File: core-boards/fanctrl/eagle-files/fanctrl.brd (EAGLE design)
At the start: 50.8 x 50.8 mm, 31 parts, among them J1 3-PIN_2MM-H, U1 MCP9701T-E/TT

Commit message: Fix typo: ISCP --> ICSP.
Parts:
- JP1: value ISCP -> ICSP
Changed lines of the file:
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@@
 <attribute name="SPICEPREFIX" value="R" x="16.875" y="42.75" size="1.778" layer="27" rot="R270" display="off"/>
 </element>
-<element name="JP1" library="pinhead" library_urn="urn:adsk.eagle:library:325" package="2X03" package3d_urn="urn:adsk.eagle:package:22462/2" value="ISCP" x="47" y="21.6" smashed="yes" rot="R90">
+<element name="JP1" library="pinhead" library_urn="urn:adsk.eagle:library:325" package="2X03" package3d_urn="urn:adsk.eagle:package:22462/2" value="ICSP" x="47" y="21.6" smashed="yes" rot="R90">
 <attribute name="NAME" x="44.32" y="25.905" size="0.6096" layer="25" ratio="10"/>
 <attribute name="POPULARITY" value="62" x="47" y="21.6" size="1.778" layer="27" rot="R90" display="off"/>

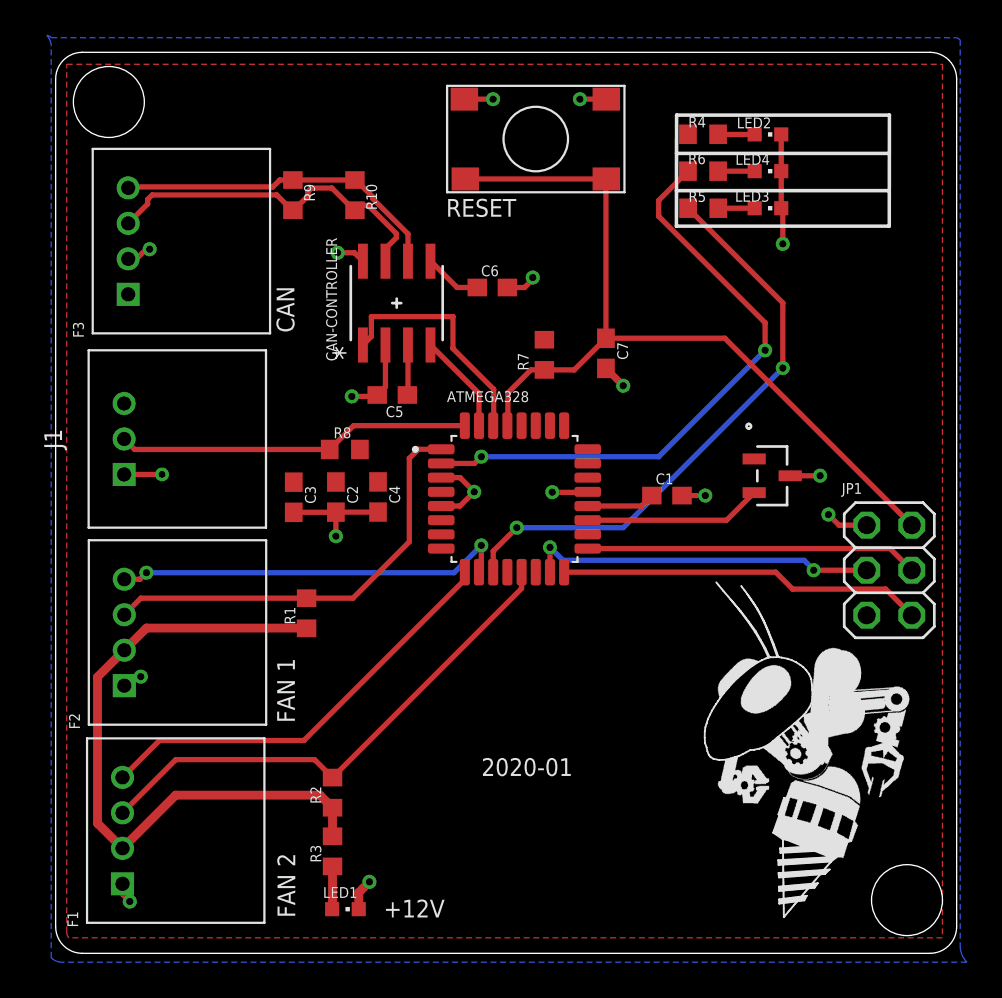
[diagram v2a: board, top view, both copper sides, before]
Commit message: Jank jumper for CAN resistor added.
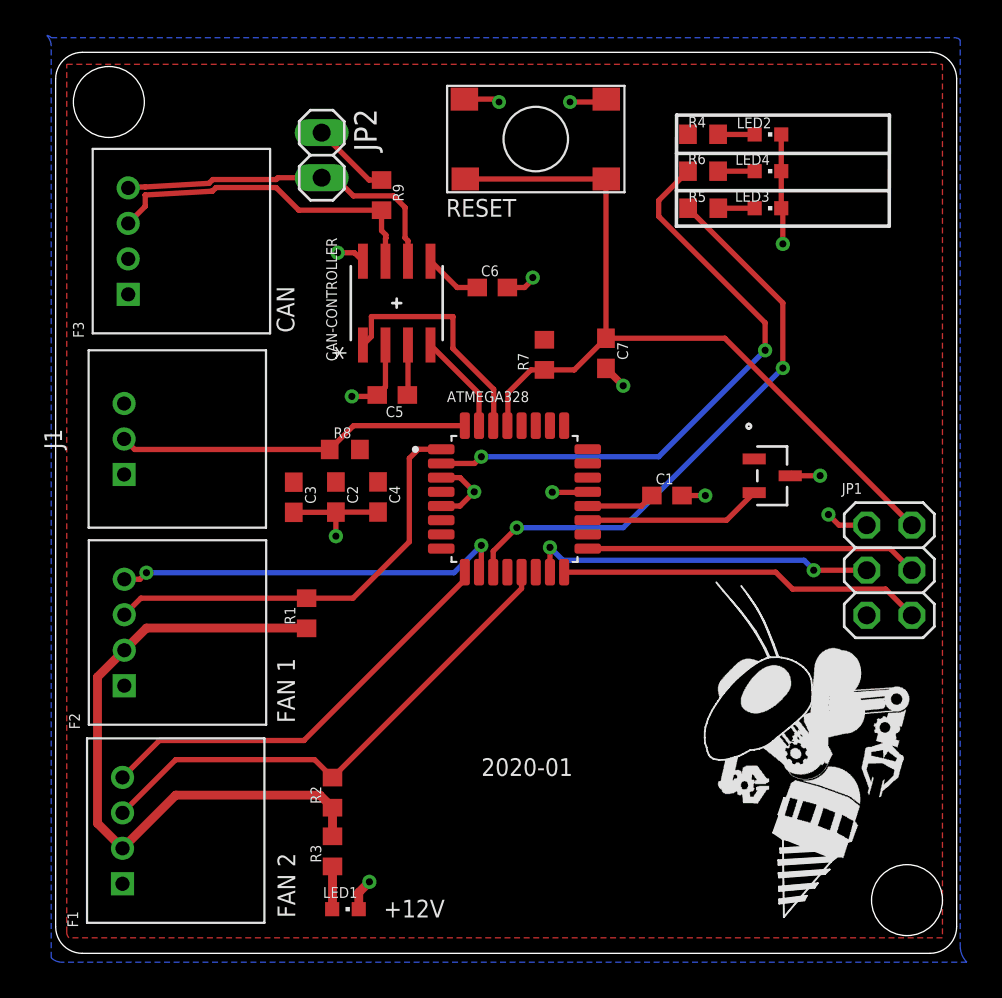
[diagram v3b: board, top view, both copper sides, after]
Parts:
- removed R10: 120Ω, rcl:R0603
- added JP2: (no value), pinhead:1X02
- moved R9 5.00 mm to (18.4, 42.8)
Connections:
- new net N$1: JP2.1, R9.1
- net CAN_N: now also JP2.2; no longer R10.1, R9.1
- net CAN_P: no longer R10.2
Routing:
- net GND: track 44.6 -> 39.7 mm, vias 18 -> 14
- net N$1: track 0.00 -> 4.48 mm
- net CAN_P: track 20.1 -> 18.9 mm
- net CAN_N: track 18.8 -> 18.0 mm

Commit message: Fix LED Resist. values --> 470ohm
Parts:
- R3: value 2.2K -> 470Ω
- R4, R5, R6: value 1K -> 470Ω
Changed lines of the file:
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@@
 <attribute name="SPICEPREFIX" value="C" x="18.175" y="25.73" size="1.778" layer="27" rot="R270" display="off"/>
 </element>
-<element name="R3" library="rcl" library_urn="urn:adsk.eagle:library:334" package="R0603" package3d_urn="urn:adsk.eagle:package:23555/3" value="2.2K" x="15.61" y="5.75" smashed="yes" rot="R90">
+<element name="R3" library="rcl" library_urn="urn:adsk.eagle:library:334" package="R0603" package3d_urn="urn:adsk.eagle:package:23555/3" value="470Ω" x="15.61" y="5.75" smashed="yes" rot="R90">
 <attribute name="NAME" x="14.975" y="5.115" size="0.6096" layer="25" rot="R90"/>
 <attribute name="POPULARITY" value="77" x="15.61" y="5.75" size="1.778" layer="27" rot="R90" display="off"/>
 <attribute name="SPICEPREFIX" value="R" x="15.61" y="5.75" size="1.778" layer="27" rot="R90" display="off"/>
 </element>
-<element name="R4" library="rcl" library_urn="urn:adsk.eagle:library:334" package="R0603" package3d_urn="urn:adsk.eagle:package:23555/3" value="1K" x="36.5" y="46.18" smashed="yes" rot="R180">
+<element name="R4" library="rcl" library_urn="urn:adsk.eagle:library:334" package="R0603" package3d_urn="urn:adsk.eagle:package:23555/3" value="470Ω" x="36.5" y="46.18" smashed="yes" rot="R180">
 <attribute name="NAME" x="35.665" y="46.565" size="0.6096" layer="25"/>
 <attribute name="POPULARITY" value="77" x="36.5" y="46.18" size="1.778" layer="27" rot="R180" display="off"/>
@@
 <attribute name="POPULARITY" value="28" x="40.16" y="46.17" size="1.778" layer="27" rot="R270" display="off"/>
 </element>
-<element name="R5" library="rcl" library_urn="urn:adsk.eagle:library:334" package="R0603" package3d_urn="urn:adsk.eagle:package:23555/3" value="1K" x="36.51" y="42.01" smashed="yes" rot="R180">
+<element name="R5" library="rcl" library_urn="urn:adsk.eagle:library:334" package="R0603" package3d_urn="urn:adsk.eagle:package:23555/3" value="470Ω" x="36.51" y="42.01" smashed="yes" rot="R180">
 <attribute name="NAME" x="35.675" y="42.365" size="0.6096" layer="25"/>
 <attribute name="POPULARITY" value="77" x="36.51" y="33.12" size="1.778" layer="27" rot="R180" display="off"/>
@@
 <attribute name="POPULARITY" value="28" x="43.97" y="47.09" size="1.778" layer="27" rot="R270" display="off"/>
 </element>
-<element name="R6" library="rcl" library_urn="urn:adsk.eagle:library:334" package="R0603" package3d_urn="urn:adsk.eagle:package:23555/3" value="1K" x="36.5" y="44.1" smashed="yes" rot="R180">
+<element name="R6" library="rcl" library_urn="urn:adsk.eagle:library:334" package="R0603" package3d_urn="urn:adsk.eagle:package:23555/3" value="470Ω" x="36.5" y="44.1" smashed="yes" rot="R180">
 <attribute name="NAME" x="35.655" y="44.495" size="0.6096" layer="25"/>
 <attribute name="POPULARITY" value="77" x="36.5" y="37.75" size="1.778" layer="27" rot="R180" display="off"/>

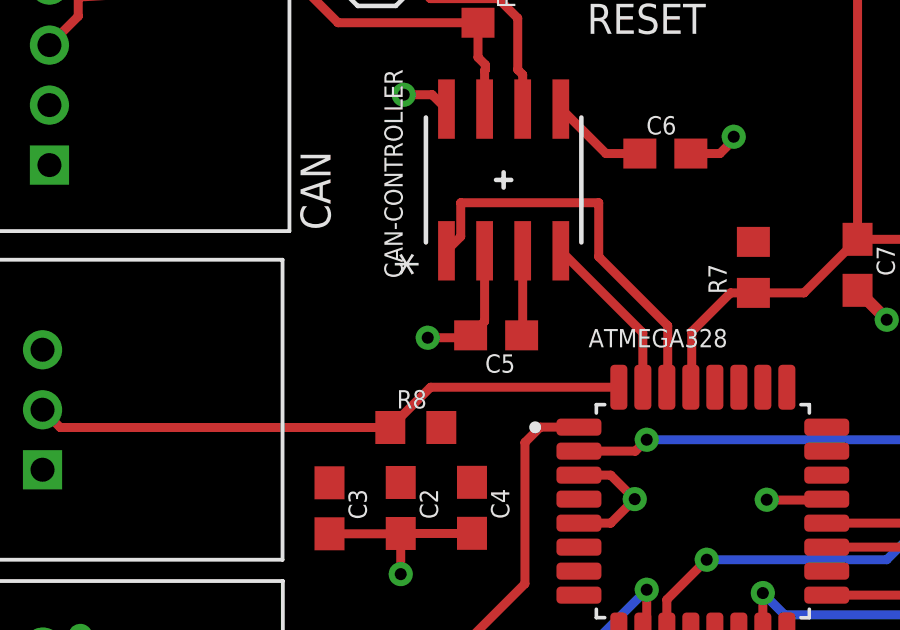
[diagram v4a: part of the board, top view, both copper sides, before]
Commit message: Add 3A fuse to +5V from CAN bus.
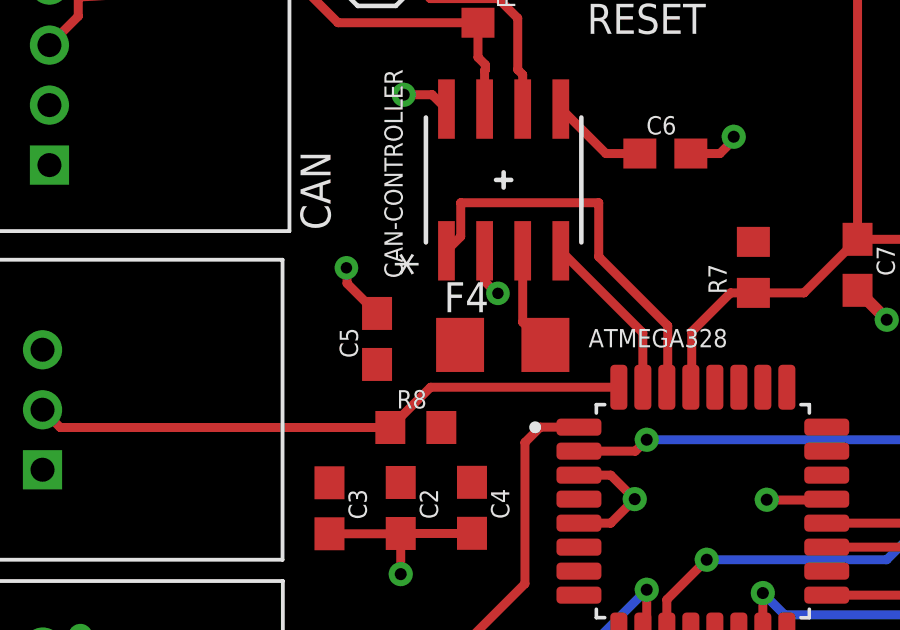
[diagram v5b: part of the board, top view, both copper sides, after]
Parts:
- added F4: 3A, RoboJackets-Fuses:F1206
- moved C5 3.97 mm to (15.0, 31.4), turned to 90 degrees
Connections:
- new net N$6: CAN-CONTROLLER.3, F4.2
- net +5V: now also F4.1; no longer CAN-CONTROLLER.3
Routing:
- net N$6: track 0.00 -> 3.45 mm
- net +5V: track 2.83 -> 0.00 mm
- net GND: track 39.7 -> 39.3 mm, vias 14 -> 15
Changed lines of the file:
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@@
 <attribute name="VENDOR" value="Microchip" x="19.23" y="36.66" size="1.778" layer="27" rot="R90" display="off"/>
 </element>
-<element name="C5" library="rcl" library_urn="urn:adsk.eagle:library:334" package="C0603" package3d_urn="urn:adsk.eagle:package:23616/2" value="0.1µF" x="18.98" y="31.48" smashed="yes" rot="R180">
-<attribute name="NAME" x="19.615" y="30.845" size="0.6096" layer="25" rot="R180"/>
-<attribute name="POPULARITY" value="37" x="18.98" y="31.48" size="1.778" layer="27" rot="R180" display="off"/>
-<attribute name="SPICEPREFIX" value="C" x="18.98" y="31.48" size="1.778" layer="27" rot="R180" display="off"/>
+<element name="C5" library="rcl" library_urn="urn:adsk.eagle:library:334" package="C0603" package3d_urn="urn:adsk.eagle:package:23616/2" value="0.1µF" x="15.01" y="31.36" smashed="yes" rot="R90">
+<attribute name="NAME" x="14.375" y="30.725" size="0.6096" layer="25" rot="R90"/>
+<attribute name="POPULARITY" value="37" x="15.01" y="31.36" size="1.778" layer="27" rot="R90" display="off"/>
+<attribute name="SPICEPREFIX" value="C" x="15.01" y="31.36" size="1.778" layer="27" rot="R90" display="off"/>
 </element>
 <element name="C6" library="rcl" library_urn="urn:adsk.eagle:library:334" package="C0603" package3d_urn="urn:adsk.eagle:package:23616/2" value="0.1µF" x="24.62" y="37.54" smashed="yes">
@@
 <attribute name="SPICEPREFIX" value="B" x="15" y="45" size="1.778" layer="27" rot="R270" display="off"/>
 <attribute name="VALUE" x="11.825" y="47.54" size="1.27" layer="27" rot="R270"/>
+</element>
+<element name="F4" library="RoboJackets-Fuses" package="F1206" value="3A" x="19.2" y="31.16" smashed="yes">
+<attribute name="NAME" x="17.24" y="32.25" size="1" layer="25"/>
 </element>
 </elements>
@@
 <wire x1="26.9" y1="38" x2="26.9" y2="38.1" width="0.3" layer="1"/>
 <via x="26.9" y="38.1" extent="1-16" drill="0.4"/>
-<wire x1="18.13" y1="31.48" x2="18.05" y2="31.4" width="0.3" layer="1"/>
-<via x="16.7" y="31.4" extent="1-16" drill="0.4"/>
-<wire x1="18.05" y1="31.4" x2="16.7" y2="31.4" width="0.3" layer="1"/>
 <wire x1="13.425" y1="24.865" x2="15.69" y2="24.865" width="0.3" layer="1"/>
 <wire x1="15.74" y1="24.815" x2="15.69" y2="24.865" width="0.3" layer="1"/>
@@
 <wire x1="35.315" y1="25.81" x2="36.63" y2="25.81" width="0.3" layer="1"/>
 <via x="36.63" y="25.81" extent="1-16" drill="0.4"/>
-<wire x1="18.595" y1="34.2978" x2="18.595" y2="31.945" width="0.3" layer="1"/>
-<wire x1="18.595" y1="31.945" x2="18.13" y2="31.48" width="0.3" layer="1"/>
+<wire x1="18.595" y1="34.2978" x2="18.725" y2="34.1678" width="0.3" layer="1"/>
+<wire x1="18.725" y1="34.1678" x2="18.725" y2="33.885" width="0.3" layer="1"/>
 <wire x1="40.91" y1="46.17" x2="40.91" y2="44.1" width="0.3" layer="1"/>
 <wire x1="40.91" y1="44.1" x2="40.91" y2="42.01" width="0.3" layer="1"/>
@@
 <wire x1="30.885" y1="48" x2="29" y2="48" width="0.3" layer="1"/>
 <via x="29" y="48" extent="1-16" drill="0.381"/>
+<wire x1="15.01" y1="32.21" x2="14.01" y2="33.21" width="0.3" layer="1"/>
+<wire x1="14.01" y1="33.21" x2="14.01" y2="33.73" width="0.3" layer="1"/>
+<wire x1="14.01" y1="33.73" x2="13.99" y2="33.73" width="0.3" layer="1"/>
+<via x="13.99" y="33.73" extent="1-16" drill="0.381"/>
+<wire x1="18.595" y1="34.2978" x2="18.595" y2="33.285" width="0.3" layer="1"/>
+<wire x1="18.595" y1="33.285" x2="19.02" y2="32.86" width="0.3" layer="1"/>
+<wire x1="19.02" y1="32.86" x2="19.04" y2="32.88" width="0.3" layer="1"/>
+<via x="19.04" y="32.88" extent="1-16" drill="0.381"/>
+<wire x1="31.045" y1="48.16" x2="40.91" y2="46.17" width="0" layer="19" extent="1-1"/>
+<wire x1="25" y1="48" x2="29" y2="48" width="0" layer="19" extent="1-1"/>
+<wire x1="26.9" y1="38.1" x2="25" y2="48" width="0" layer="19" extent="1-1"/>
+<wire x1="31.027" y1="32.98" x2="26.9" y2="38.1" width="0" layer="19" extent="1-1"/>
+<wire x1="30" y1="26.02" x2="32" y2="32" width="0" layer="19" extent="1-1"/>
+<wire x1="23.6" y1="26.02" x2="28" y2="26" width="0" layer="19" extent="1-1"/>
+<wire x1="18.245" y1="24.95" x2="21.74" y2="25.22" width="0" layer="19" extent="1-1"/>
+<wire x1="35.315" y1="25.81" x2="30" y2="26.02" width="0" layer="19" extent="1-1"/>
+<wire x1="41.4152" y1="26.925" x2="36.63" y2="25.81" width="0" layer="19" extent="1-1"/>
+<wire x1="43.57" y1="24.74" x2="43.1" y2="26.93" width="0" layer="19" extent="1-1"/>
+<wire x1="19.04" y1="32.88" x2="21.74" y2="26.82" width="0" layer="19" extent="1-1"/>
+<wire x1="15.01" y1="32.21" x2="18.725" y2="33.885" width="0" layer="19" extent="1-1"/>
+<wire x1="17.325" y1="39.0222" x2="18.595" y2="34.2978" width="0" layer="19" extent="1-1"/>
+<wire x1="3.86" y1="27" x2="13.425" y2="24.865" width="0" layer="19" extent="1-1"/>
+<wire x1="4.09" y1="39.155" x2="13.99" y2="33.73" width="0" layer="19" extent="1-1"/>
+<wire x1="3.87" y1="15.09" x2="3.86" y2="27" width="0" layer="19" extent="1-1"/>
+<wire x1="3.77" y1="3.92" x2="3.87" y2="15.09" width="0" layer="19" extent="1-1"/>
+<wire x1="17.09" y1="2.49" x2="3.77" y2="3.92" width="0" layer="19" extent="1-1"/>
 </signal>
 <signal name="FAN2-PWM-OUT">
@@
 <contactref element="C4" pad="1"/>
 <contactref element="R4" pad="2"/>
-<contactref element="CAN-CONTROLLER" pad="3"/>
 <contactref element="C5" pad="1"/>
 <contactref element="U1" pad="1"/>
@@
 <vertex x="0.625" y="1.176778125"/>
 </polygon>
-<wire x1="19.865" y1="34.2978" x2="19.865" y2="31.515" width="0.3" layer="1"/>
-<wire x1="19.865" y1="31.515" x2="19.83" y2="31.48" width="0.3" layer="1"/>
 <contactref element="J1" pad="3"/>
+<contactref element="F4" pad="1"/>
 </signal>
 <signal name="ANALOG-TEMP-READING">
@@
 <wire x1="17.67" y1="43.6" x2="18.375" y2="43.6" width="0.3" layer="1"/>
 </signal>
+<signal name="N$6">
+<contactref element="CAN-CONTROLLER" pad="3"/>
+<contactref element="F4" pad="2"/>
+<wire x1="19.865" y1="34.2978" x2="19.865" y2="31.917" width="0.3" layer="1"/>
+<wire x1="19.865" y1="31.917" x2="20.622" y2="31.16" width="0.3" layer="1"/>
+</signal>
 </signals>

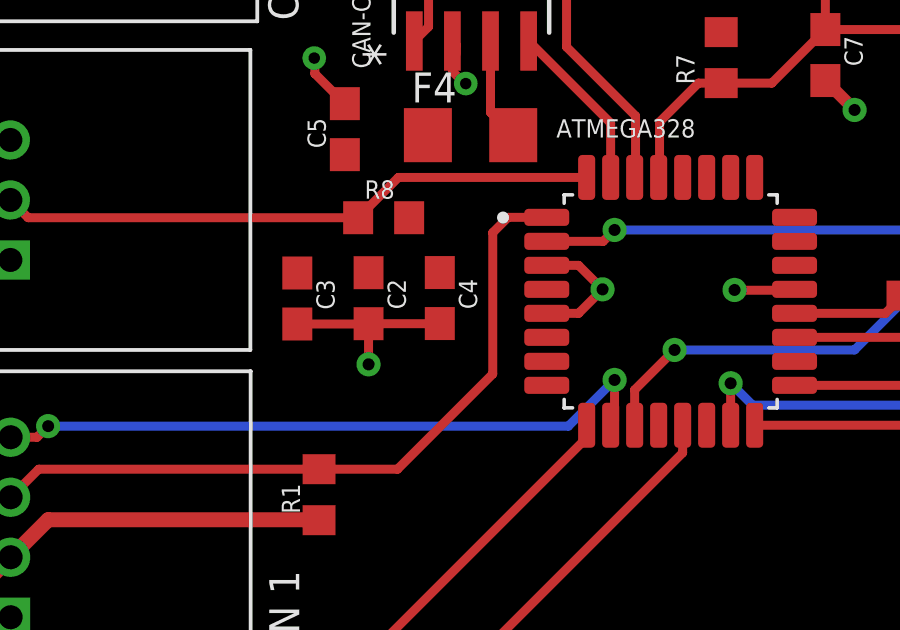
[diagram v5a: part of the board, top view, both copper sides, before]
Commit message: One ground per power pin on the ATMega.
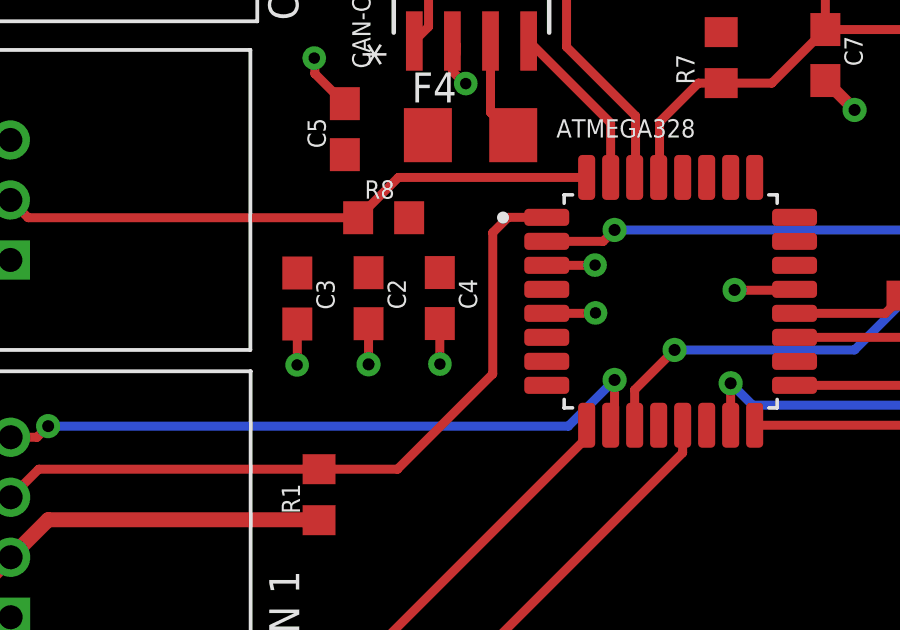
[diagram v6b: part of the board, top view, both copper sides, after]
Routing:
- net GND: track 39.3 -> 36.3 mm, vias 15 -> 18
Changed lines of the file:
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@@
 <wire x1="26.9" y1="38" x2="26.9" y2="38.1" width="0.3" layer="1"/>
 <via x="26.9" y="38.1" extent="1-16" drill="0.4"/>
-<wire x1="13.425" y1="24.865" x2="15.69" y2="24.865" width="0.3" layer="1"/>
 <wire x1="15.74" y1="24.815" x2="15.69" y2="24.865" width="0.3" layer="1"/>
-<wire x1="18.17" y1="24.875" x2="15.8" y2="24.875" width="0.3" layer="1"/>
 <wire x1="18.17" y1="24.875" x2="18.175" y2="24.88" width="0.3" layer="1"/>
 <wire x1="30" y1="26.02" x2="29.97" y2="25.99" width="0.3" layer="1"/>
@@
 <via x="28" y="26" extent="1-16" drill="0.4"/>
 <wire x1="29.97" y1="25.99" x2="28.01" y2="25.99" width="0.3" layer="1"/>
-<via x="23.6" y="26.02" extent="1-16" drill="0.4"/>
-<wire x1="21.74" y1="25.22" x2="22.8" y2="25.22" width="0.3" layer="1"/>
-<wire x1="22.8" y1="25.22" x2="23.6" y2="26.02" width="0.3" layer="1"/>
-<wire x1="21.74" y1="26.82" x2="22.8" y2="26.82" width="0.3" layer="1"/>
-<wire x1="22.8" y1="26.82" x2="23.6" y2="26.02" width="0.3" layer="1"/>
 <wire x1="45.73" y1="24.14" x2="44.17" y2="24.14" width="0.3" layer="1"/>
 <wire x1="44.17" y1="24.14" x2="43.57" y2="24.74" width="0.3" layer="1"/>
@@
 <wire x1="19.02" y1="32.86" x2="19.04" y2="32.88" width="0.3" layer="1"/>
 <via x="19.04" y="32.88" extent="1-16" drill="0.381"/>
+<wire x1="23.34" y1="26.82" x2="23.35" y2="26.83" width="0.3" layer="1"/>
+<via x="23.35" y="26.83" extent="1-16" drill="0.381"/>
+<wire x1="21.74" y1="26.82" x2="23.34" y2="26.82" width="0.3" layer="1"/>
+<wire x1="23.32" y1="25.22" x2="23.35" y2="25.25" width="0.3" layer="1"/>
+<wire x1="23.35" y1="25.25" x2="23.365" y2="25.235" width="0.3" layer="1"/>
+<via x="23.365" y="25.235" extent="1-16" drill="0.381"/>
+<wire x1="21.74" y1="25.22" x2="23.32" y2="25.22" width="0.3" layer="1"/>
+<wire x1="13.425" y1="24.865" x2="13.425" y2="23.505" width="0.3" layer="1"/>
+<wire x1="13.425" y1="23.505" x2="13.42" y2="23.5" width="0.3" layer="1"/>
+<via x="13.42" y="23.5" extent="1-16" drill="0.381"/>
+<wire x1="18.175" y1="24.88" x2="18.175" y2="23.535" width="0.3" layer="1"/>
+<wire x1="18.175" y1="23.535" x2="18.18" y2="23.53" width="0.3" layer="1"/>
+<via x="18.18" y="23.53" extent="1-16" drill="0.381"/>
 <wire x1="31.045" y1="48.16" x2="40.91" y2="46.17" width="0" layer="19" extent="1-1"/>
 <wire x1="25" y1="48" x2="29" y2="48" width="0" layer="19" extent="1-1"/>
@@
 <wire x1="31.027" y1="32.98" x2="26.9" y2="38.1" width="0" layer="19" extent="1-1"/>
 <wire x1="30" y1="26.02" x2="32" y2="32" width="0" layer="19" extent="1-1"/>
-<wire x1="23.6" y1="26.02" x2="28" y2="26" width="0" layer="19" extent="1-1"/>
+<wire x1="23.365" y1="25.235" x2="28" y2="26" width="0" layer="19" extent="1-1"/>
+<wire x1="23.35" y1="26.83" x2="23.365" y2="25.235" width="0" layer="19" extent="1-1"/>
 <wire x1="18.245" y1="24.95" x2="21.74" y2="25.22" width="0" layer="19" extent="1-1"/>
+<wire x1="15.8" y1="24.875" x2="18.175" y2="24.88" width="0" layer="19" extent="1-1"/>
+<wire x1="13.425" y1="24.865" x2="15.69" y2="24.865" width="0" layer="19" extent="1-1"/>
 <wire x1="35.315" y1="25.81" x2="30" y2="26.02" width="0" layer="19" extent="1-1"/>
 <wire x1="41.4152" y1="26.925" x2="36.63" y2="25.81" width="0" layer="19" extent="1-1"/>
